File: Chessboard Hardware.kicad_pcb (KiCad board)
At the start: 2 copper layers, 200 x 200 mm, 74 parts, among them IC1 SS49E, IC10 SS49E, IC11 SS49E, IC12 SS49E, IC13 SS49E, IC14 SS49E, IC15 SS49E, IC16 SS49E, IC17 SS49E, IC18 SS49E, IC19 SS49E, IC2 SS49E, IC20 SS49E, IC21 SS49E, IC22 SS49E, IC23 SS49E, IC24 SS49E, IC25 SS49E, IC26 SS49E, IC27 SS49E, IC28 SS49E, IC29 SS49E, IC3 SS49E, IC30 SS49E, IC31 SS49E, IC32 SS49E, IC33 SS49E, IC34 SS49E, IC35 SS49E, IC36 SS49E, IC37 SS49E, IC38 SS49E, IC39 SS49E, IC4 SS49E, IC40 SS49E, IC41 SS49E, IC42 SS49E, IC43 SS49E, IC44 SS49E, IC45 SS49E, IC46 SS49E, IC47 SS49E, IC48 SS49E, IC49 SS49E, IC5 SS49E, IC50 SS49E, IC51 SS49E, IC52 SS49E, IC53 SS49E, IC54 SS49E, IC55 SS49E, IC56 SS49E, IC57 SS49E, IC58 SS49E, IC59 SS49E, IC6 SS49E, IC60 SS49E, IC61 SS49E, IC62 SS49E, IC63 SS49E, IC64 SS49E, IC65 CD74HC4067M96, IC66 CD74HC4067M96, IC67 CD74HC4067M96, IC68 CD74HC4067M96, IC7 SS49E, IC8 SS49E, IC9 SS49E, J1 Conn_01x04_Pin

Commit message: Everything except linear halls routed
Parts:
- A1, J1: moved to B.Cu
- moved A1 95.9 mm to (217.2, 92.6)
- moved J1 89.3 mm to (248.2, 59.4)
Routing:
- net GND: track 0.00 -> 1781.6 mm
- net VCC: track 0.00 -> 1672.9 mm
- net /S3: track 0.00 -> 272.1 mm, vias 0 -> 5
- net /EN: track 0.00 -> 265.8 mm, vias 0 -> 5
- net /S2: track 0.00 -> 263.4 mm, vias 0 -> 5
- net /S1: track 0.00 -> 244.0 mm, vias 0 -> 5
- net /COM3: track 0.00 -> 239.6 mm
- net /S0: track 0.00 -> 237.2 mm, vias 0 -> 5
- net /COM2: track 0.00 -> 191.2 mm
- net /COM1: track 0.00 -> 110.7 mm
- net /COM0: track 0.00 -> 79.1 mm
- net /SDA: track 0.00 -> 25.5 mm
- net /SCL: track 0.00 -> 25.2 mm

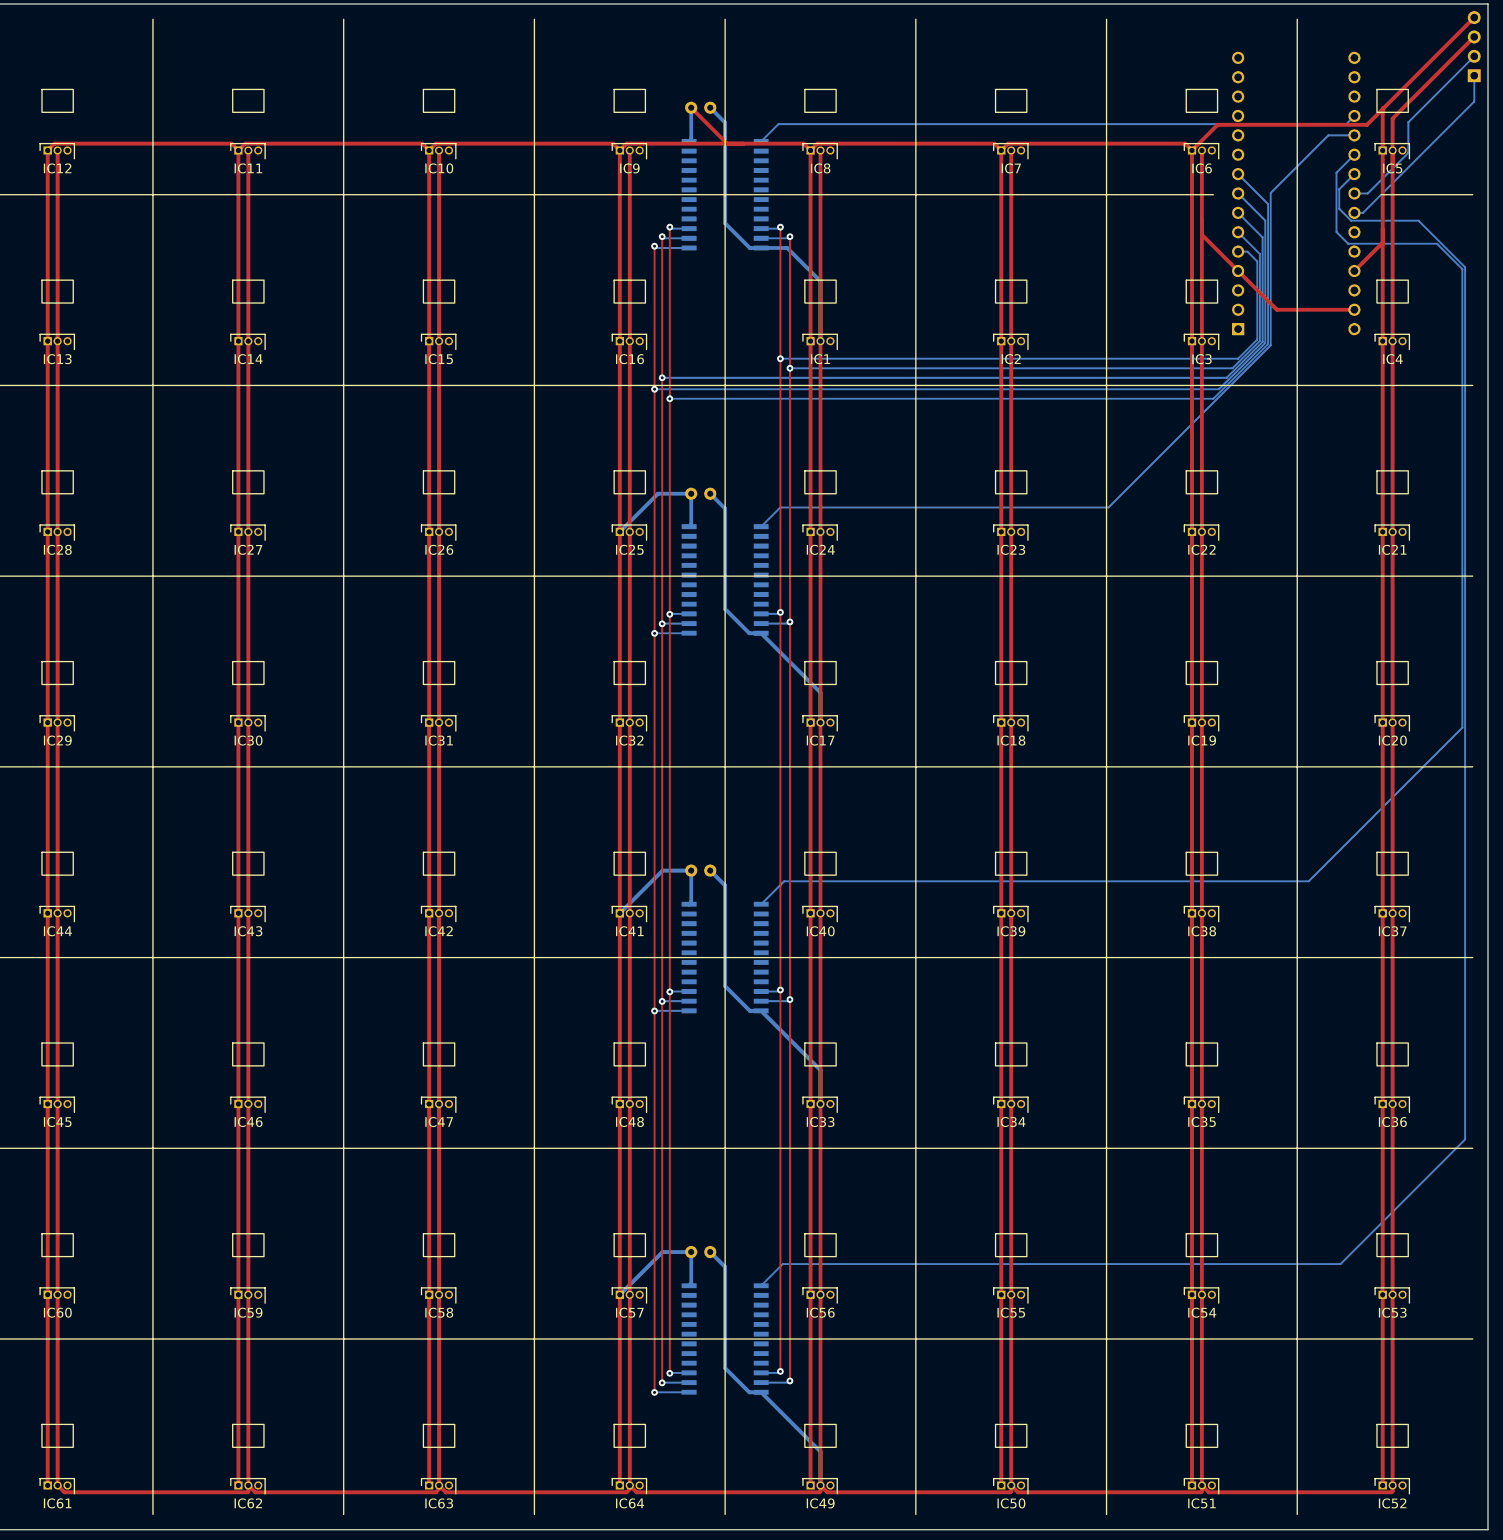
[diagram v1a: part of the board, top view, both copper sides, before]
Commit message: Autoroute and cleanup linear hall traces
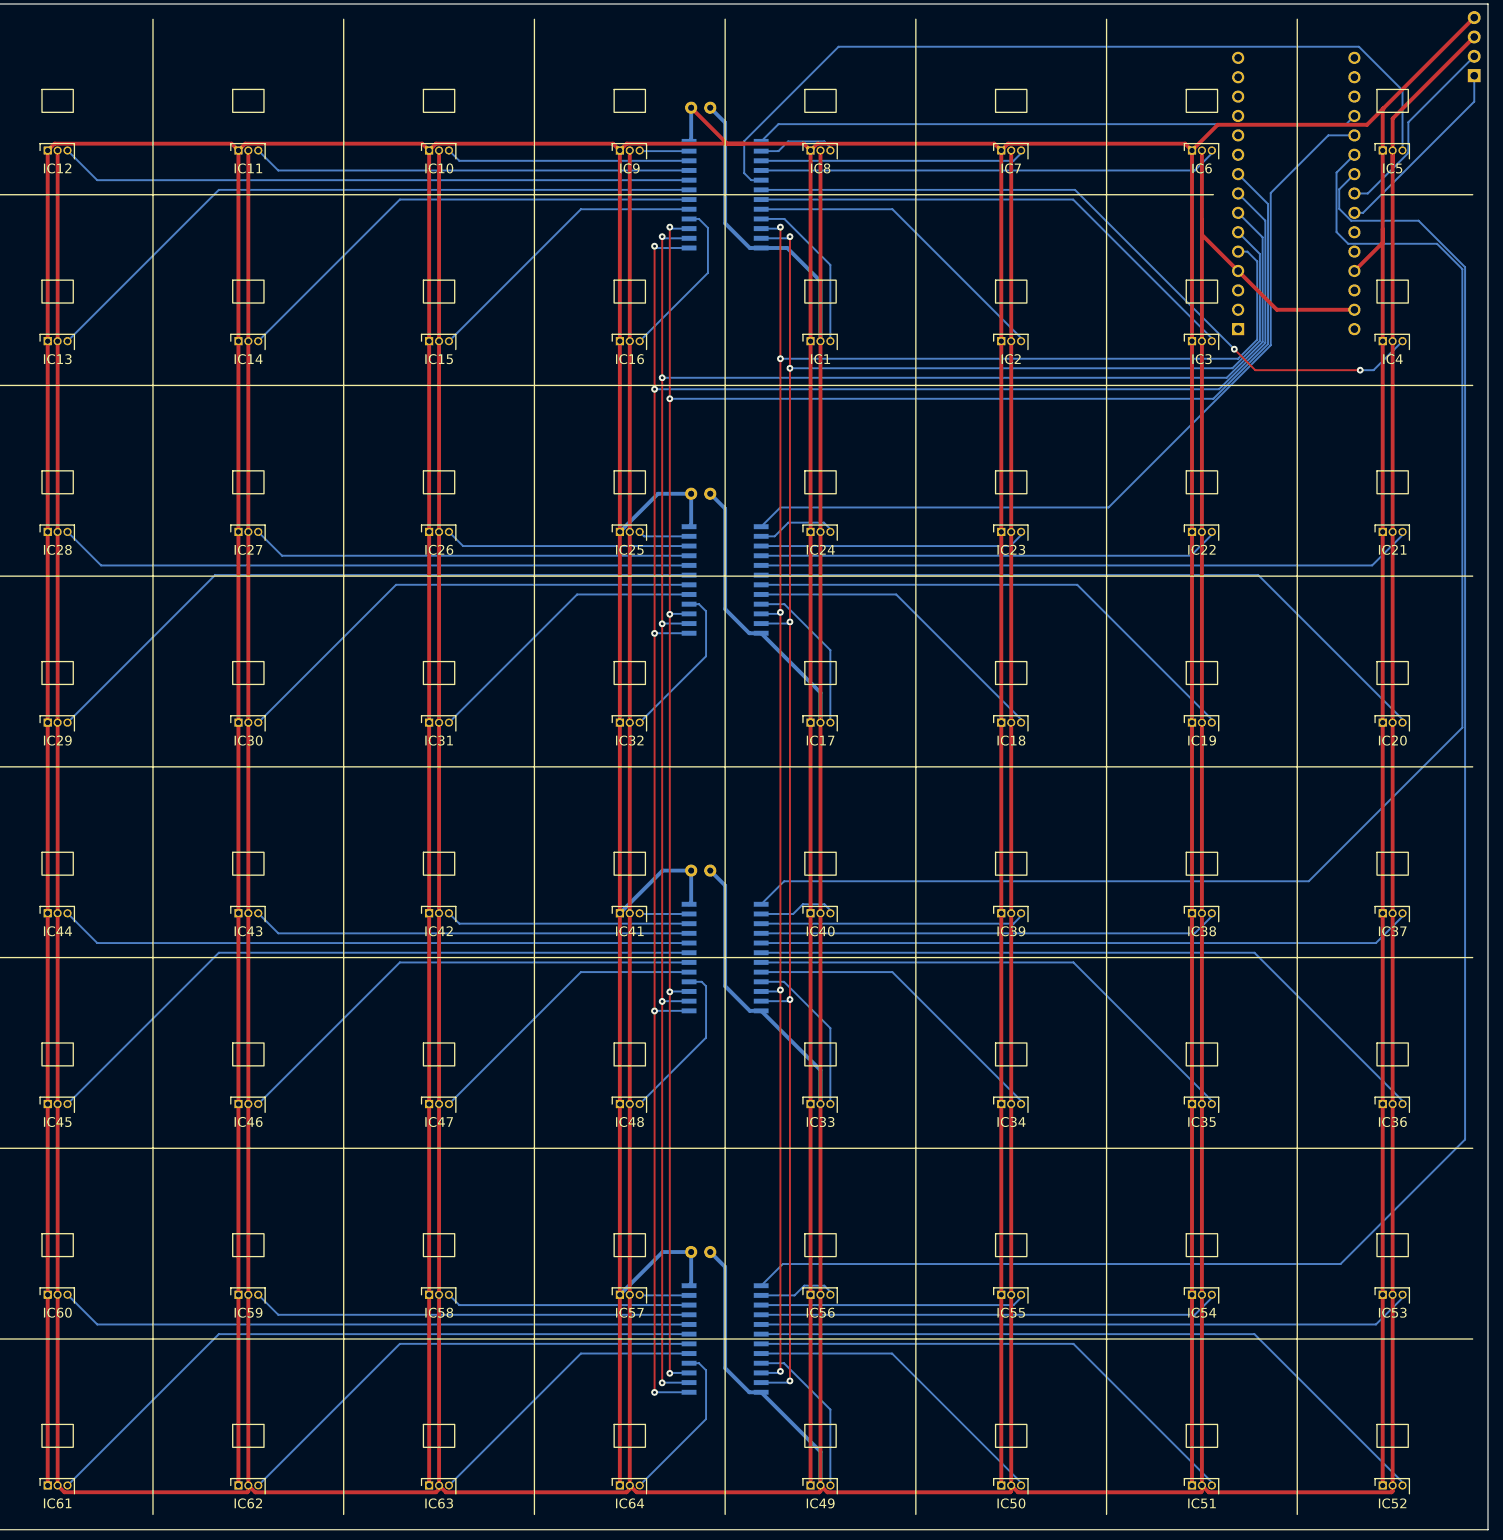
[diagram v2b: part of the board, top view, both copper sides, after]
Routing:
- net Net-(IC5-O): track 0.00 -> 108.5 mm
- net Net-(IC4-O): track 0.00 -> 95.4 mm, vias 0 -> 2
- net Net-(IC52-O): track 0.00 -> 92.5 mm
- net Net-(IC36-O): track 0.00 -> 92.5 mm
- net Net-(IC20-O): track 0.00 -> 92.3 mm
- net Net-(IC13-O): track 0.00 -> 89.7 mm
- net Net-(IC45-O): track 0.00 -> 89.7 mm
- net Net-(IC61-O): track 0.00 -> 89.7 mm
- net Net-(IC29-O): track 0.00 -> 89.5 mm
- net Net-(IC21-O): track 0.00 -> 86.1 mm
- net Net-(IC53-O): track 0.00 -> 85.9 mm
- net Net-(IC37-O): track 0.00 -> 85.9 mm
- net Net-(IC28-O): track 0.00 -> 83.3 mm
- net Net-(IC60-O): track 0.00 -> 83.1 mm
- net Net-(IC44-O): track 0.00 -> 83.1 mm
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
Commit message: Done
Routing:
- added copper zone on F.Cu, net GND
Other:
- board text added: "For CD74HC4067M96 Dot in top left"
- board text added: "For SS49E Flat side down"
- board text added: "GND"
- board text added: "SCL"
- board text added: "SDA"
- board text added: "VCC"
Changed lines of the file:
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@@
 		(tags "Through hole pin header THT 1x04 2.54mm single row")
 		(property "Reference" "J1"
-			(at 0 2.33 0)
+			(at 0 2.85 0)
 			(unlocked yes)
 			(layer "B.SilkS")
@@
 		(layer "Edge.Cuts")
 	)
+	(gr_text "GND"
+		(at 246.5 55 -0)
+		(layer "B.SilkS")
+		(effects
+			(font
+				(size 1.27 1.27)
+				(thickness 0.3)
+				(bold yes)
+			)
+			(justify left bottom mirror)
+		)
+	)
+	(gr_text "SDA"
+		(at 246.5 57.75 -0)
+		(layer "B.SilkS")
+		(effects
+			(font
+				(size 1.27 1.27)
+				(thickness 0.3)
+				(bold yes)
+			)
+			(justify left bottom mirror)
+		)
+	)
+	(gr_text "SCL"
+		(at 246.5 60.25 -0)
+		(layer "B.SilkS")
+		(effects
+			(font
+				(size 1.27 1.27)
+				(thickness 0.3)
+				(bold yes)
+			)
+			(justify left bottom mirror)
+		)
+	)
+	(gr_text "For CD74HC4067M96\nDot in top left"
+		(at 150 59 -0)
+		(layer "B.SilkS")
+		(effects
+			(font
+				(size 1.524 1.524)
+				(thickness 0.3048)
+				(bold yes)
+			)
+			(justify bottom mirror)
+		)
+	)
+	(gr_text "VCC"
+		(at 246.5 52.5 -0)
+		(layer "B.SilkS")
+		(effects
+			(font
+				(size 1.27 1.27)
+				(thickness 0.3)
+				(bold yes)
+			)
+			(justify left bottom mirror)
+		)
+	)
+	(gr_text "For SS49E\nFlat side down"
+		(at 62.5 60 0)
+		(layer "F.SilkS")
+		(effects
+			(font
+				(size 1.524 1.524)
+				(thickness 0.3048)
+				(bold yes)
+			)
+			(justify bottom)
+		)
+	)
 	(segment
 		(start 186.2 69.2)
@@
 		(net 93)
 	)
+	(zone
+		(net 25)
+		(net_name "GND")
+		(layer "F.Cu")
+		(hatch edge 0.5)
+		(connect_pads
+			(clearance 0.508)
+		)
+		(min_thickness 0.25)
+		(filled_areas_thickness no)
+		(fill yes
+			(thermal_gap 0.5)
+			(thermal_bridge_width 0.5)
+		)
+		(polygon
+			(pts
+				(xy 50 50) (xy 250 50) (xy 250 250) (xy 50 250)
+			)
+		)
+	)
 )

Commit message: Done and Gerbers
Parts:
- added TP1: TestPoint, SamacSys_PCB_Library_KiCad:TestPoint, F.Cu at (132.2, 103.4)
- added TP10: TestPoint, SamacSys_PCB_Library_KiCad:TestPoint, F.Cu at (127.4, 62.9)
- added TP11: TestPoint, SamacSys_PCB_Library_KiCad:TestPoint, F.Cu at (131.6, 62.9)
- added TP2: TestPoint, SamacSys_PCB_Library_KiCad:TestPoint, F.Cu at (132.2, 108.5)
- added TP3: TestPoint, SamacSys_PCB_Library_KiCad:TestPoint, F.Cu at (132.2, 113.5)
- added TP4: TestPoint, SamacSys_PCB_Library_KiCad:TestPoint, F.Cu at (132.2, 118.5)
- added TP5: TestPoint, SamacSys_PCB_Library_KiCad:TestPoint, F.Cu at (223.0, 105.5)
- added TP6: TestPoint, SamacSys_PCB_Library_KiCad:TestPoint, F.Cu at (223.0, 110.8)
- added TP7: TestPoint, SamacSys_PCB_Library_KiCad:TestPoint, F.Cu at (223.0, 115.7)
- added TP8: TestPoint, SamacSys_PCB_Library_KiCad:TestPoint, F.Cu at (223.0, 120.7)
- added TP9: TestPoint, SamacSys_PCB_Library_KiCad:TestPoint, F.Cu at (146.9, 105.0)
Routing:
- net /COM0: track 79.1 -> 148.1 mm
- net /S0: track 237.2 -> 286.2 mm
- net /S1: track 244.0 -> 284.0 mm
- net /COM3: track 239.6 -> 271.5 mm, vias 0 -> 2
- net /COM2: track 191.2 -> 218.0 mm
- net /S2: track 263.4 -> 285.7 mm
- net /COM1: track 110.7 -> 129.7 mm
- net GND: track 1781.6 -> 1798.7 mm
- net /S3: track 272.1 -> 283.9 mm
- net VCC: track 1672.9 -> 1681.5 mm
- net /EN: track 265.8 -> 273.5 mm
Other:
- board text added: "COM0"
- board text added: "COM1"
- board text added: "COM2"
- board text added: "COM3"
- board text added: "EN"
- board text added: "S0"
- board text added: "S1"
- board text added: "S2"
- board text added: "S3"
